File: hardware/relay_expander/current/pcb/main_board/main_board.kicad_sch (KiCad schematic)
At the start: 12 parts, among them J1 Conn_01x07_Socket, J2 Screw_Terminal_01x02, J3 Conn_01x07_Socket, SW1 SW_DIP_x03, U1 MCP23017x-x-SO

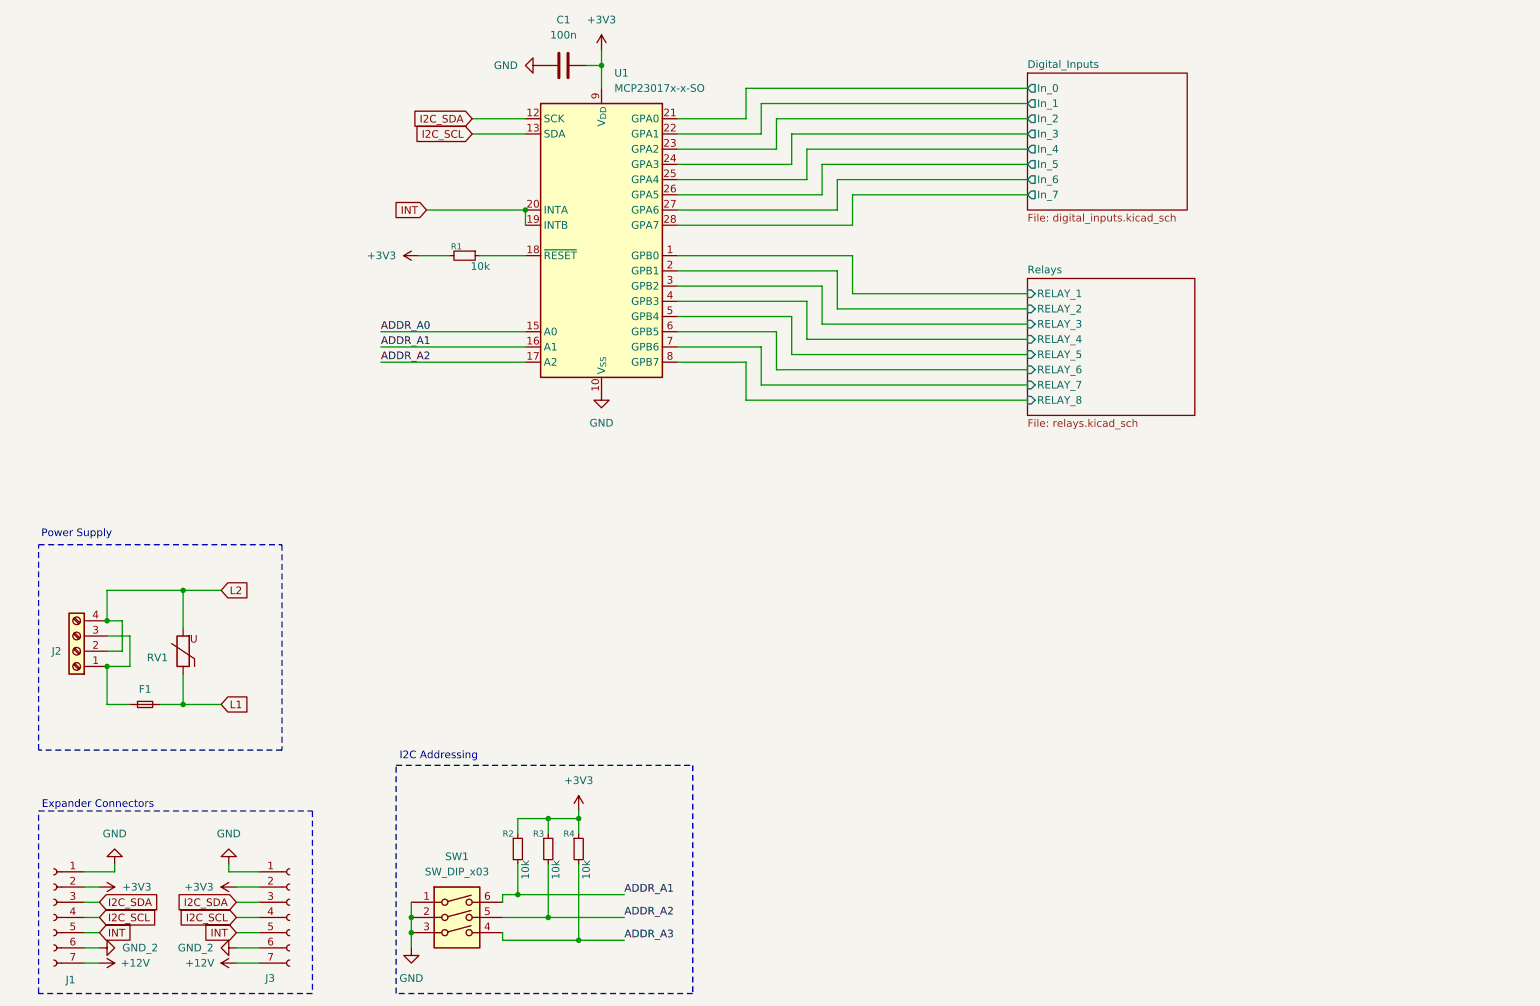
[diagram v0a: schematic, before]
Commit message: [ADD] ui board template
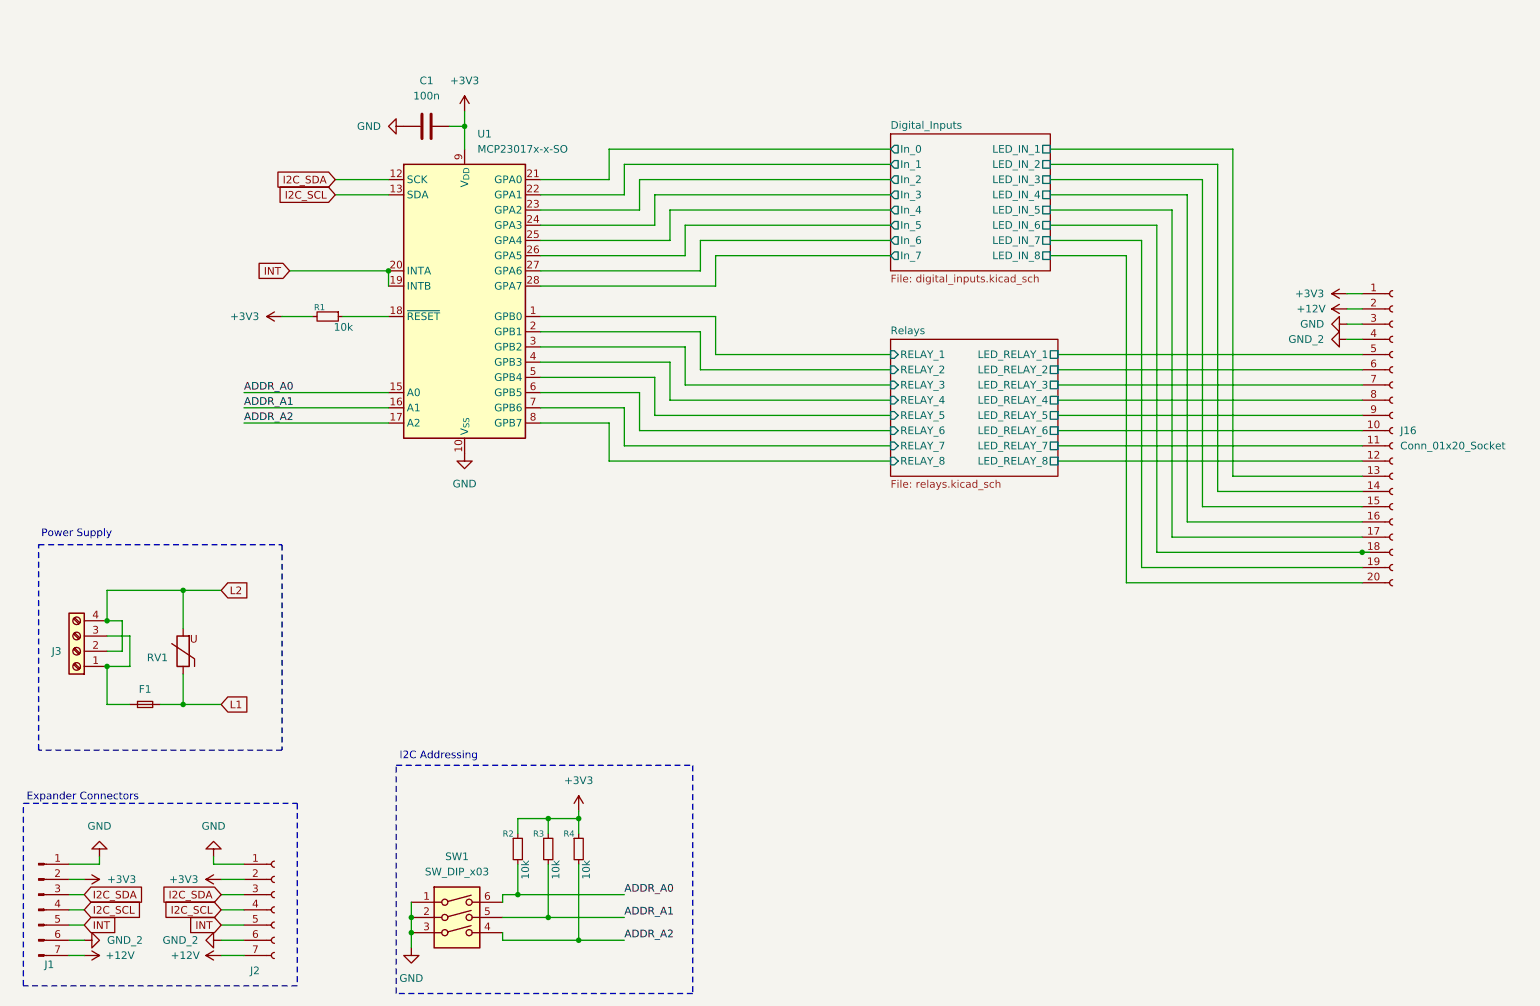
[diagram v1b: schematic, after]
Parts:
- removed J1: Conn_01x07_Socket, templates_lib_footprints:PinSocket_1x07_P2.54mm_Horizontal, symbol Connector:Conn_01x07_Socket
- removed J3: Conn_01x07_Socket, templates_lib_footprints:PinSocket_1x07_P2.54mm_Horizontal_Right, symbol Connector:Conn_01x07_Socket
- added J1: Conn_01x07_Socket, homeautomation_core:PinHeader_1x07_P2.54mm_Horizontal_left, symbol Connector:Conn_01x07_Pin
- added J16: Conn_01x20_Socket, Connector_PinSocket_1.27mm:PinSocket_2x10_P1.27mm_Vertical, symbol Connector:Conn_01x20_Socket
- added J2: Conn_01x07_Socket, homeautomation_core:PinSocket_1x07_P2.54mm_Horizontal_Right, symbol Connector:Conn_01x07_Socket
- renumbered J2 to J3
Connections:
- net ADDR_A3 is gone; now on net ADDR_A2: R4.2, SW1.4
- net +12V: now also J1.7 (Pin_7), J16.2 (Pin_2), J2.7 (Pin_7)
- net +3V3: now also J1.2 (Pin_2), J16.1 (Pin_1), J2.2 (Pin_2)
- net ADDR_A0: now also R2.2, SW1.6
- net ADDR_A1: now also R3.2, SW1.5; no longer R2.2, SW1.6
- net ADDR_A2: no longer R3.2, SW1.5
- net GND: now also J1.1 (Pin_1), J16.3 (Pin_3), J2.1 (Pin_1)
- net GND_2: now also J1.6 (Pin_6), J16.4 (Pin_4), J2.6 (Pin_6)
- net I2C_SCL: now also J1.4 (Pin_4), J2.4 (Pin_4)
- net I2C_SDA: now also J1.3 (Pin_3), J2.3 (Pin_3)
- net INT: now also J1.5 (Pin_5), J2.5 (Pin_5)
- new net Digital_Inputs/LED_IN_1: J16.13 (Pin_13)
- new net Digital_Inputs/LED_IN_2: J16.14 (Pin_14)
- new net Digital_Inputs/LED_IN_3: J16.15 (Pin_15)
- new net Digital_Inputs/LED_IN_4: J16.16 (Pin_16)
- new net Digital_Inputs/LED_IN_5: J16.17 (Pin_17)
- new net Digital_Inputs/LED_IN_6: J16.18 (Pin_18)
- new net Digital_Inputs/LED_IN_7: J16.19 (Pin_19)
- new net Digital_Inputs/LED_IN_8: J16.20 (Pin_20)
- new net Relays/LED_RELAY_1: J16.5 (Pin_5)
- new net Relays/LED_RELAY_2: J16.6 (Pin_6)
- new net Relays/LED_RELAY_3: J16.7 (Pin_7)
- new net Relays/LED_RELAY_4: J16.8 (Pin_8)
- new net Relays/LED_RELAY_5: J16.9 (Pin_9)
- new net Relays/LED_RELAY_6: J16.10 (Pin_10)
- new net Relays/LED_RELAY_7: J16.11 (Pin_11)
- new net Relays/LED_RELAY_8: J16.12 (Pin_12)
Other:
- sheet Digital_Inputs ports: added LED_IN_1, LED_IN_2, LED_IN_3, LED_IN_4, LED_IN_5, LED_IN_6, LED_IN_7, LED_IN_8; removed none
- sheet Relays ports: added LED_RELAY_1, LED_RELAY_2, LED_RELAY_3, LED_RELAY_4, LED_RELAY_5, LED_RELAY_6, LED_RELAY_7, LED_RELAY_8; removed none
- moved on the sheet: C1, R1, U1
